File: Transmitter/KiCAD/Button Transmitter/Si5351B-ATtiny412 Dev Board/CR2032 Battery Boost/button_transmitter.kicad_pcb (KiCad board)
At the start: 2 copper layers, 24.4 x 24.4 mm, 35 parts, among them J1 1.27mm Pogo Pads, J2 Conn_Coaxial, Q1 MMUN2238LT1G, U1 ATtiny412-SS, U2 Si5351B-B-GM1, U3 TLV61070ADBV, Y1 25MHz

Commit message: Finished CR2032 PCB layout
I like this. This is good
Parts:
- removed the J1 at (72.6, 94.2)
- added BZ2-1: 7BB-20-3, Library:Buzzer_Pad_NEG, B.Cu at (72.6, 93.0)
- added C8: 100nF, Library:Worthington_C_0402_1005Metric, F.Cu at (72.9, 106.6)
- added J2: 1.27mm Pogo Pads For Programming & Debug, Library:2x3_1.27mm_Pogo_Header, F.Cu at (75.8, 115.0)
- added U5: TLV61070ADBV, Package_TO_SOT_SMD:SOT-23-6, F.Cu at (74.6, 111.5)
- BT1: footprint Battery:BatteryHolder_Keystone_3034_1x20mm -> Library:BatteryHolder_Keystone_3034_1x20mm_CUTOUT
- BZ1: value Buzzer Pads -> 7BB-20-3; footprint Jumper:SolderJumper-2_P1.3mm_Open_RoundedPad1.0x1.5mm -> Library:Buzzer_Pad_POS
- C1, C4, C5, C6, C7: footprint Resistor_SMD:R_0402_1005Metric -> Library:Worthington_C_0402_1005Metric
- C10: value 10uF -> 22uF; footprint Resistor_SMD:R_0402_1005Metric -> Capacitor_SMD:C_0603_1608Metric
- C2: value 10uF -> 100nF; footprint Resistor_SMD:R_0402_1005Metric -> Library:Worthington_C_0402_1005Metric
- C3: value 100nF -> 10uF; footprint Resistor_SMD:R_0402_1005Metric -> Library:Worthington_C_0402_1005Metric
- C9: value 22uF -> 10uF; footprint Resistor_SMD:R_0603_1608Metric -> Library:Worthington_C_0402_1005Metric
- D1, D3: footprint LED_SMD:LED_0402_1005Metric -> Library:Worthington_LED_0402_1005Metric
- D2: value LS0504EVT233 -> ESD156B1W; footprint Package_TO_SOT_SMD:SOT-23-3 -> Diode_SMD:D_0201_0603Metric
- J1: renamed from J2; value Conn_Coaxial -> Antenna Screw Pad
- L1: value 220uH -> 100mH; footprint Inductor_SMD:L_1008_2520Metric -> Inductor_THT:L_Axial_L12.0mm_D5.0mm_P15.24mm_Horizontal_Fastron_MISC
- R1: value 1k8 -> 10k; footprint Resistor_SMD:R_0402_1005Metric -> Library:Worthington_R_0402_1005Metric
- R10, R11, R5, R6, R7, R9: footprint Resistor_SMD:R_0402_1005Metric -> Library:Worthington_R_0402_1005Metric
- R3: value 0R -> 1k8; footprint Resistor_SMD:R_0402_1005Metric -> Resistor_SMD:R_0603_1608Metric
- R4: value 10k -> 0R; footprint Resistor_SMD:R_0402_1005Metric -> Library:Worthington_R_0402_1005Metric
- R8: value 100 -> 220; footprint Resistor_SMD:R_0402_1005Metric -> Library:Worthington_R_0402_1005Metric
- U1: value ATtiny412-SS -> TPS22919DCK; footprint Package_SO:SOIC-8_3.9x4.9mm_P1.27mm -> Package_TO_SOT_SMD:SOT-363_SC-70-6
- U3: value TLV61070ADBV -> ATtiny416-M; footprint Package_TO_SOT_SMD:SOT-23-6 -> Package_DFN_QFN:VQFN-20-1EP_3x3mm_P0.4mm_EP1.7x1.7mm
- U4: value ~ -> Case
- moved BZ1 21.4 mm to (78.6, 93.0), turned to 180 degrees
- moved L1 18.6 mm to (68.0, 95.8), turned to 0 degrees
- moved Q1 18.1 mm to (66.6, 100.5), turned to -90 degrees
- moved C1 17.3 mm to (83.9, 107.5), turned to -135 degrees
- moved C5 14.7 mm to (69.3, 109.6), turned to -90 degrees
- moved C4 14.1 mm to (67.7, 107.8), turned to 135 degrees
- moved R1 13.6 mm to (75.6, 92.2), turned to 180 degrees
- moved R5 12.3 mm to (75.6, 94.3)
- moved U1 12.1 mm to (78.3, 109.1)
- moved C2 11.0 mm to (77.9, 106.9), turned to 180 degrees
- moved C6 9.77 mm to (75.6, 93.2)
- moved U2 9.61 mm to (81.6, 105.6), turned to -135 degrees
- moved R9 8.08 mm to (80.0, 112.1), turned to -90 degrees
- moved C3 7.62 mm to (80.7, 108.9), turned to -45 degrees
- moved R6 6.97 mm to (65.3, 102.3), turned to 90 degrees
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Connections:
- C1 pad 1: +3V3 -> /+3V3_SW
- C10 pad 1: Net-(D2-OUT) -> +3V3
- C2 pad 1: +3V3 -> /+3V3_SW
- C3 pad 1: +3V3 -> /+3V3_SW
- C6 pad 1: GND -> Net-(C6-Pad1)
- C6 pad 2: /~{TX_EN} -> Net-(BZ1-+)
- C7 pad 1: Net-(C7-Pad1) -> GND
- C7 pad 2: Net-(BZ1-+) -> /MCU_DAC0
- C9 pad 1: +3V3 -> Net-(BT1-+)
- D1 pad 2: Net-(D1-A) -> /BUZZER_PULSE
- J1 pad 1: /CLK3 -> /CLK1
- L1 pad 1: Net-(C7-Pad1) -> Net-(C6-Pad1)
- L1 pad 2: +3V3 -> /+3V3_SW
- L2 pad 1: Net-(D2-OUT) -> Net-(BT1-+)
- L2 pad 2: Net-(U3-SW) -> Net-(U5-SW)
- R1 pad 1: +3V3 -> Net-(BZ1-+)
- R1 pad 2: /MCU_SDA -> GND
- R10 pad 1: Net-(U3-V_{FB}) -> Net-(U5-V_{FB})
- R2 pad 1: +3V3 -> /+3V3_SW
- R3 pad 1: /CLK3_T -> /+3V3_SW
- R3 pad 2: /CLK3 -> /MCU_SDA
- R4 pad 1: Net-(BZ1-+) -> /CLK1_T
- R4 pad 2: GND -> /CLK1
- R5 pad 2: Net-(C7-Pad1) -> Net-(C6-Pad1)
- R6 pad 1: Net-(D1-A) -> /BUZZER_PULSE
- R9 pad 2: Net-(U3-V_{FB}) -> Net-(U5-V_{FB})
- U1 pad 2: /MCU_DAC0 -> GND
- U1 pad 3: Net-(D1-A) -> /OUTPUT_PWR_EN
- U1 pad 4: /MCU_SDA -> (no net)
- U1 pad 5: /MCU_SCL -> /+3V3_SW
- U1 pad 6: /MCU_UPDI -> /+3V3_SW
- U2 pad 11: +3V3 -> /+3V3_SW
- U2 pad 12: /CLK3_T -> unconnected-(U2-CLK3-Pad12)
- U2 pad 14: +3V3 -> /+3V3_SW
- U2 pad 16: +3V3 -> /+3V3_SW
- U2 pad 7: unconnected-(U2-CLK1-Pad7) -> /CLK1_T
- U2 pad 8: +3V3 -> /+3V3_SW
- U2 pad 9: +3V3 -> /+3V3_SW
- U3 pad 1: Net-(U3-SW) -> unconnected-(U3-PA2-Pad1)
- U3 pad 2: GND -> unconnected-(U3-PA3-Pad2)
- U3 pad 3: Net-(D2-OUT) -> GND
- U3 pad 4: Net-(U3-V_{FB}) -> +3V3
- U3 pad 5: +3V3 -> unconnected-(U3-PA4-Pad5)
- U3 pad 6: Net-(D2-OUT) -> /OUTPUT_PWR_EN
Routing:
- net +3V3: track 122.8 -> 31.2 mm, vias 9 -> 0
- net /+3V3_SW: track 0.00 -> 53.9 mm, vias 0 -> 1
- net GND: track 125.6 -> 77.7 mm, vias 15 -> 30
- net /MCU_DAC0: track 23.3 -> 52.9 mm, vias 4 -> 3
- net /MCU_SCL: track 23.7 -> 38.9 mm, vias 3 -> 2
- net Net-(Q1-G): track 16.1 -> 2.63 mm
- net /MCU_UPDI: track 7.67 -> 19.4 mm
- net /OUTPUT_PWR_EN: track 0.00 -> 11.6 mm
- net /MCU_SDA: track 24.0 -> 35.4 mm
- net Net-(BT1-+): track 37.5 -> 48.9 mm
- net Net-(D2-OUT): track 10.1 -> 0.00 mm
- net Net-(C6-Pad1): track 0.00 -> 7.35 mm
- net Net-(C7-Pad1): track 5.78 -> 0.00 mm
- net /CLK3: track 5.46 -> 0.00 mm
- net /BUZZER_PULSE: track 0.00 -> 5.11 mm
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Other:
- board size 24.4 x 24.4 mm -> 25 x 25 mm

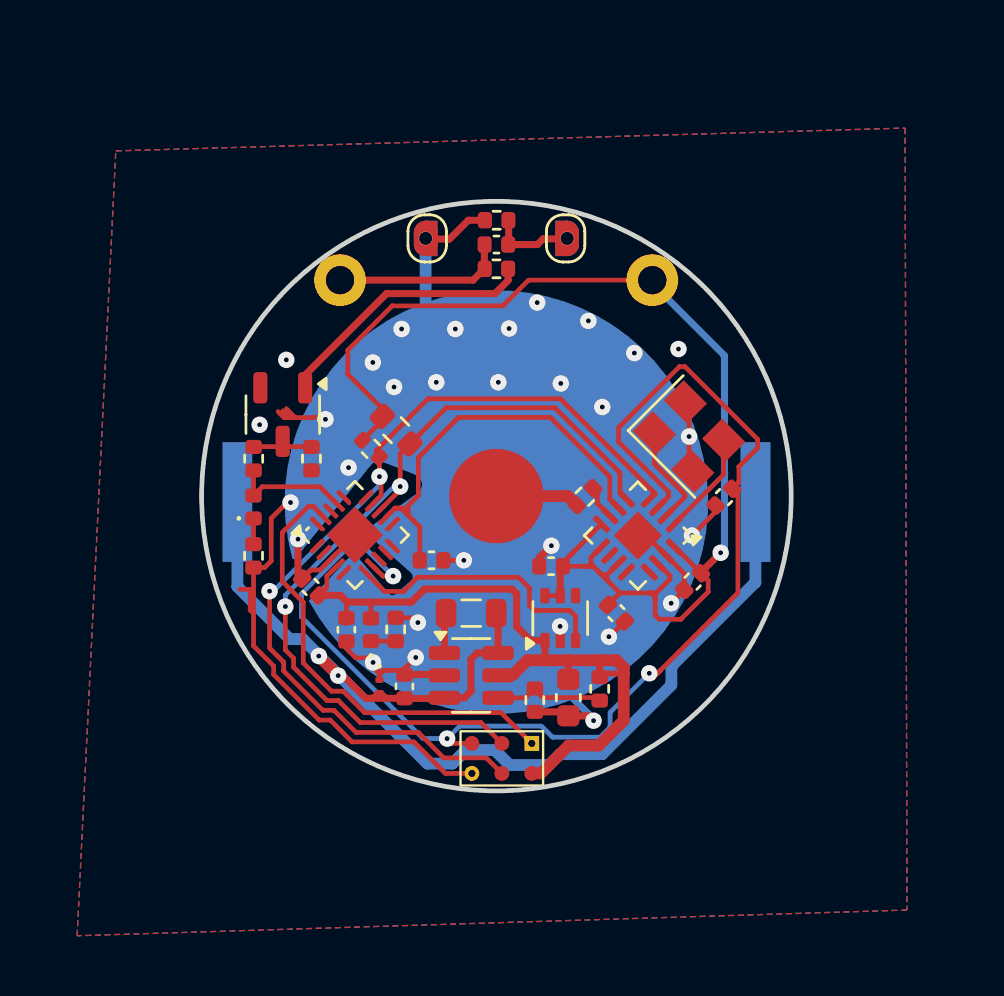
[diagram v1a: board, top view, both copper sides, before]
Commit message: Added logos to silkscreen
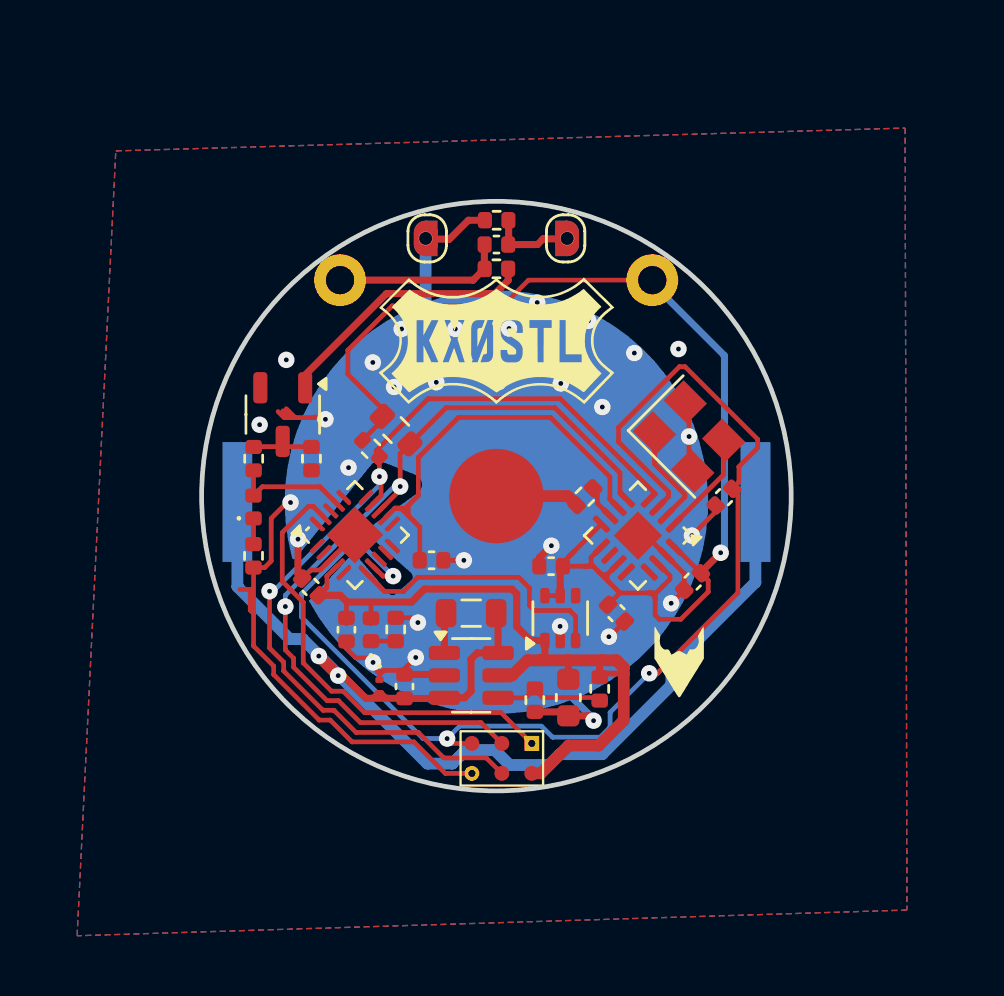
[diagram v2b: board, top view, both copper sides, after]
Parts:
- added G***: LOGO, Library:Logo_10mm_inv, F.Cu at (75.6, 97.3)
- added G***: LOGO, Library:IPL_Logo_3mm, F.Cu at (83.4, 111.0)
